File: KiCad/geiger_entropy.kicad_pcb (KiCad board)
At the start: 2 copper layers, 114.5 x 130.5 mm, 34 parts, among them J1 AudioJack2, J2 Jack-DC, J3 ICSP, J4 Conn_01x04_Socket, J5 Conn_01x10_Pin, J6 Conn_01x10_Pin, SW1 RESET, SW2 REV, SW3 FWD, U1 LM393, U2 L7805, U4 ATmega328-P, Y1 16MHz

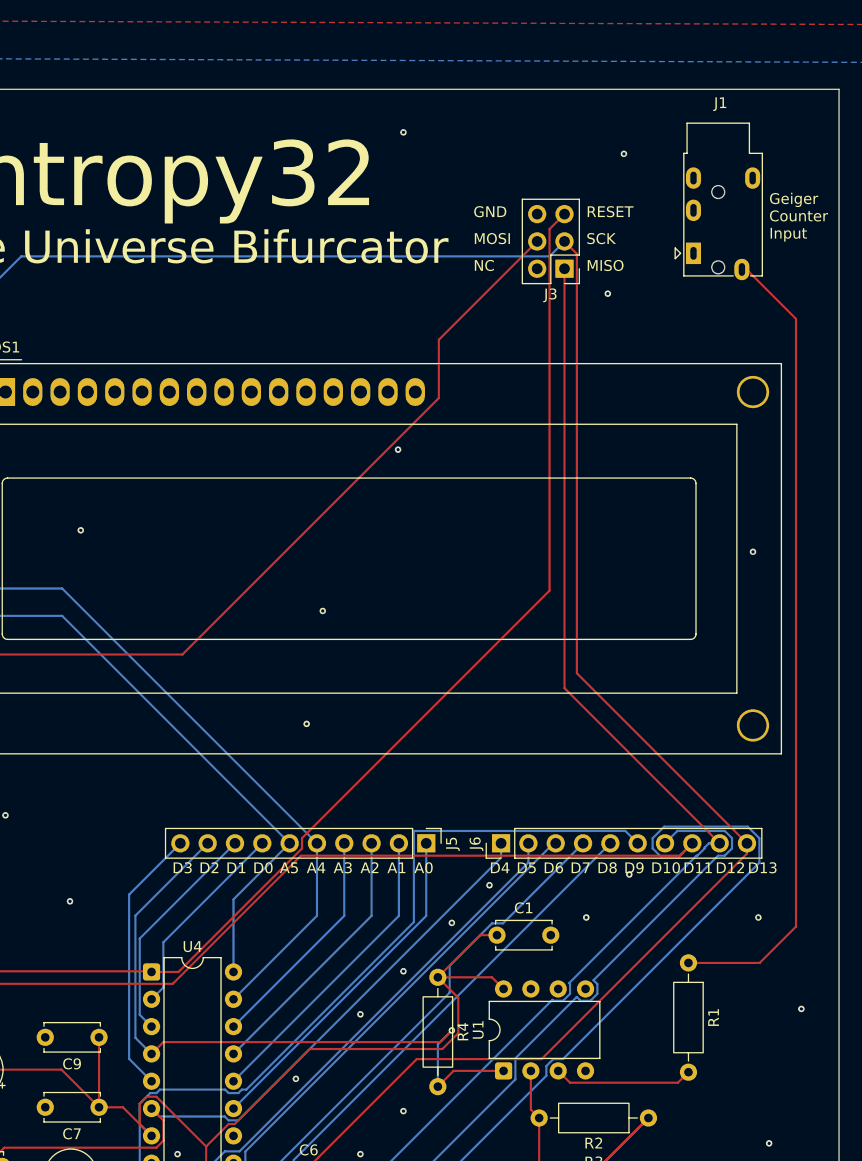
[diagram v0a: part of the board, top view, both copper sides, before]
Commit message: Add BOM and fix signal line debounce issue with a 100pF capacitor - optimise PCB layout
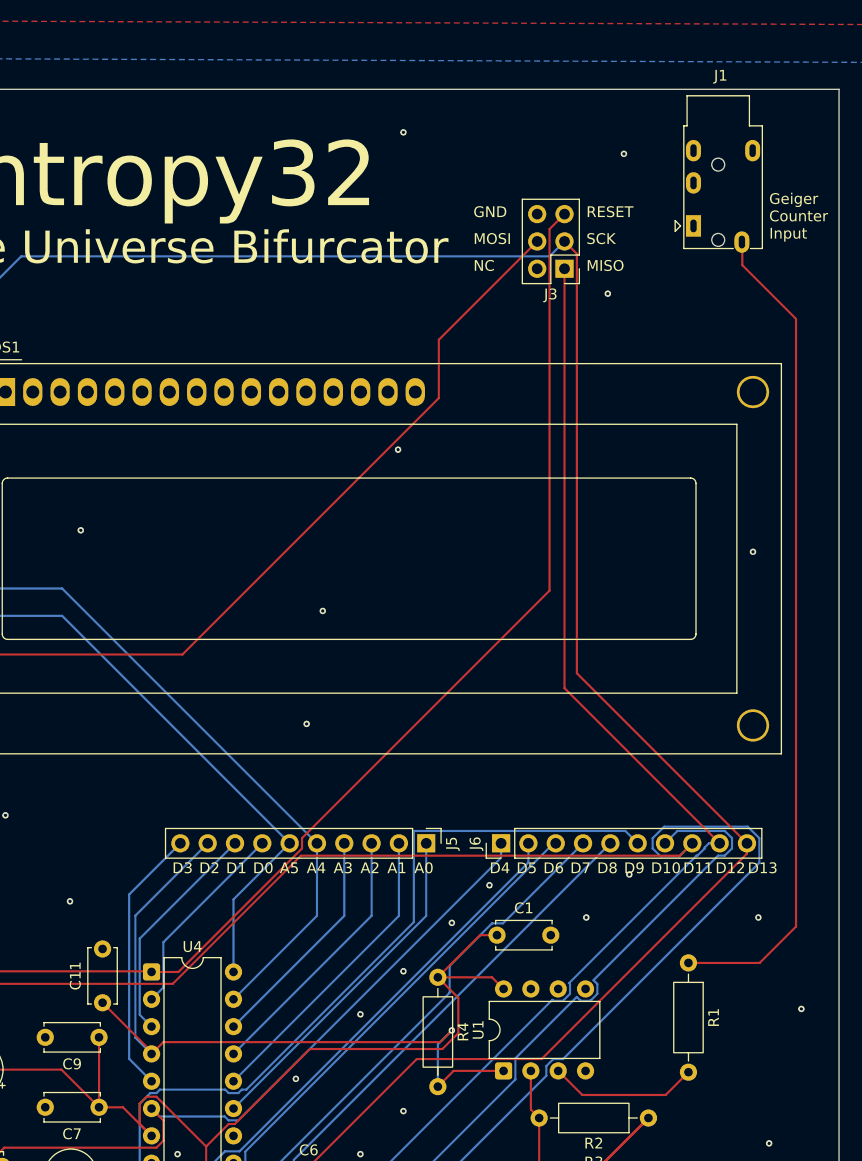
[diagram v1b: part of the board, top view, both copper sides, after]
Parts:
- added C11: 100pF, Capacitor_THT:C_Disc_D5.0mm_W2.5mm_P5.00mm, F.Cu at (79.0, 112.9)
- moved J1 2.55 mm to (134.0, 40.7)
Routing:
- net /D2: track 64.3 -> 70.9 mm
- net Net-(J1-PadS): track 74.8 -> 77.1 mm
- net /Geiger_pulse: track 13.0 -> 13.9 mm
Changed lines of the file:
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@@
 	(footprint "Capacitor_THT:C_Disc_D5.0mm_W2.5mm_P5.00mm"
 		(layer "F.Cu")
+		(at 79.025 112.925 90)
+		(descr "C, Disc series, Radial, pin pitch=5.00mm, diameter*width=5*2.5mm^2, Capacitor, http://cdn-reichelt.de/documents/datenblatt/B300/DS_KERKO_TC.pdf")
+		(tags "C Disc series Radial pin pitch 5.00mm diameter 5mm width 2.5mm Capacitor")
+		(property "Reference" "C11"
+			(at 2.5 -2.5 90)
+			(layer "F.SilkS")
+			(effects
+				(font
+					(size 1 1)
+					(thickness 0.15)
+				)
+			)
+		)
+		(property "Value" "100pF"
+			(at 2.5 2.5 90)
+			(layer "F.Fab")
+			(effects
+				(font
+					(size 1 1)
+					(thickness 0.15)
+				)
+			)
+		)
+		(property "Datasheet" ""
+			(at 0 0 90)
+			(layer "F.Fab")
+			(hide yes)
+			(effects
+				(font
+					(size 1.27 1.27)
+				)
+			)
+		)
+		(property "Description" "Unpolarized capacitor"
+			(at 0 0 90)
+			(layer "F.Fab")
+			(hide yes)
+			(effects
+				(font
+					(size 1.27 1.27)
+				)
+			)
+		)
+		(property "KiLib_Generator" "capacitor/THT/other"
+			(at 0 0 90)
+			(layer "F.SilkS")
+			(hide yes)
+			(effects
+				(font
+					(size 1 1)
+					(thickness 0.15)
+				)
+			)
+		)
+		(property ki_fp_filters "C_*")
+		(sheetname "/")
+		(sheetfile "geiger_entropy.kicad_sch")
+		(units
+			(unit
+				(name "A")
+				(pins "1" "2")
+			)
+		)
+		(attr through_hole)
+		(duplicate_pad_numbers_are_jumpers no)
+		(fp_line
+			(start 5.12 -1.37)
+			(end 5.12 -1.033)
+			(stroke
+				(width 0.12)
+				(type solid)
+			)
+			(layer "F.SilkS")
+		)
+		(fp_line
+			(start -0.12 -1.37)
+			(end 5.12 -1.37)
+			(stroke
+				(width 0.12)
+				(type solid)
+			)
+			(layer "F.SilkS")
+		)
+		(fp_line
+			(start -0.12 -1.033)
+			(end -0.12 -1.37)
+			(stroke
+				(width 0.12)
+				(type solid)
+			)
+			(layer "F.SilkS")
+		)
+		(fp_line
+			(start 5.12 1.033)
+			(end 5.12 1.37)
+			(stroke
+				(width 0.12)
+				(type solid)
+			)
+			(layer "F.SilkS")
+		)
+		(fp_line
+			(start 5.12 1.37)
+			(end -0.12 1.37)
+			(stroke
+				(width 0.12)
+				(type solid)
+			)
+			(layer "F.SilkS")
+		)
+		(fp_line
+			(start -0.12 1.37)
+			(end -0.12 1.033)
+			(stroke
+				(width 0.12)
+				(type solid)
+			)
+			(layer "F.SilkS")
+		)
+		(fp_rect
+			(start -1.05 -1.5)
+			(end 6.05 1.5)
+			(stroke
+				(width 0.05)
+				(type solid)
+			)
+			(fill no)
+			(layer "F.CrtYd")
+		)
+		(fp_rect
+			(start 0 -1.25)
+			(end 5 1.25)
+			(stroke
+				(width 0.1)
+				(type solid)
+			)
+			(fill no)
+			(layer "F.Fab")
+		)
+		(fp_text user "${REFERENCE}"
+			(at 2.5 0 90)
+			(layer "F.Fab")
+			(effects
+				(font
+					(size 1 1)
+					(thickness 0.15)
+				)
+			)
+		)
+		(pad "1" thru_hole circle
+			(at 0 0 90)
+			(size 1.6 1.6)
+			(drill 0.8)
+			(layers "*.Cu" "*.Mask")
+			(remove_unused_layers no)
+			(net "/D2")
+			(pintype "passive")
+		)
+		(pad "2" thru_hole circle
+			(at 5 0 90)
+			(size 1.6 1.6)
+			(drill 0.8)
+			(layers "*.Cu" "*.Mask")
+			(remove_unused_layers no)
+			(net "GND")
+			(pintype "passive")
+		)
+		(embedded_fonts no)
+		(model "${KICAD10_3DMODEL_DIR}/Capacitor_THT.3dshapes/C_Disc_D5.0mm_W2.5mm_P5.00mm.step"
+			(offset
+				(xyz 0 0 0)
+			)
+			(scale
+				(xyz 1 1 1)
+			)
+			(rotate
+				(xyz 0 0 0)
+			)
+		)
+	)
+	(footprint "Capacitor_THT:C_Disc_D5.0mm_W2.5mm_P5.00mm"
+		(layer "F.Cu")
 		(at 69.7 128.1425 180)
 		(descr "C, Disc series, Radial, pin pitch=5.00mm, diameter*width=5*2.5mm^2, Capacitor, http://cdn-reichelt.de/documents/datenblatt/B300/DS_KERKO_TC.pdf")
@@
 	(footprint "Connector_Audio:Jack_3.5mm_PJ320E_Horizontal"
 		(layer "F.Cu")
-		(at 133.9675 43.25)
+		(at 133.9675 40.7)
 		(descr "Headphones with microphone connector, 3.5mm, 4 pins (http://www.qingpu-electronics.com/en/products/WQP-PJ320E-177.html)")
 		(tags "3.5mm jack mic microphone phones headphones 4pins audio plug")
@@
 	)
 	(segment
+		(start 79.025 112.925)
+		(end 83.58 117.48)
+		(width 0.2)
+		(layer "F.Cu")
+		(net "/D2")
+	)
+	(segment
 		(start 111.5 115.5)
 		(end 110.4175 116.5825)
@@
 	)
 	(segment
+		(start 83.58 117.48)
+		(end 83.58 117.6825)
+		(width 0.2)
+		(layer "F.Cu")
+		(net "/D2")
+	)
+	(segment
 		(start 110.4175 116.5825)
 		(end 84.68 116.5825)
@@
 	)
 	(segment
-		(start 138.4675 44.75)
-		(end 138.9075 44.75)
+		(start 143.5 105.8425)
+		(end 140.12 109.2225)
 		(width 0.2)
 		(layer "F.Cu")
@@
 	)
 	(segment
-		(start 133.5 109.2225)
-		(end 140.12 109.2225)
+		(start 138.5 44.3425)
+		(end 143.5 49.3425)
 		(width 0.2)
 		(layer "F.Cu")
@@
 	)
 	(segment
-		(start 143.5 49.3425)
-		(end 143.5 105.8425)
+		(start 140.12 109.2225)
+		(end 133.5 109.2225)
 		(width 0.2)
 		(layer "F.Cu")
@@
 	)
 	(segment
-		(start 138.9075 44.75)
-		(end 143.5 49.3425)
+		(start 138.4675 42.2)
+		(end 138.5 42.2325)
 		(width 0.2)
 		(layer "F.Cu")
@@
 	)
 	(segment
-		(start 140.12 109.2225)
+		(start 138.5 42.2325)
+		(end 138.5 44.3425)
+		(width 0.2)
+		(layer "F.Cu")
+		(net "Net-(J1-PadS)")
+	)
+	(segment
+		(start 143.5 49.3425)
 		(end 143.5 105.8425)
 		(width 0.2)
@@
 	)
 	(segment
-		(start 133.5 119.3825)
-		(end 132.52 120.3625)
+		(start 123.6275 121.5)
+		(end 121.39 119.2625)
 		(width 0.2)
 		(layer "F.Cu")
@@
 	)
 	(segment
-		(start 122.49 120.3625)
-		(end 121.39 119.2625)
+		(start 131.3825 121.5)
+		(end 123.6275 121.5)
 		(width 0.2)
 		(layer "F.Cu")
@@
 	)
 	(segment
-		(start 132.52 120.3625)
-		(end 122.49 120.3625)
+		(start 133.5 119.3825)
+		(end 131.3825 121.5)
 		(width 0.2)
 		(layer "F.Cu")

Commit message: Update PCB
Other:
- board text added: "CAUTION: TRUE RANDOMNESS INSIDE OPERATION MAY CAUSE PARALLEL UNIVERSES"
- board text added: "This device complies with the Heisenberg Uncertainty Principle. Operation is subject to the following: (1) this device may not cause harmful interference with causality, (2) this device must accept any interference received, including unexpected entropy."
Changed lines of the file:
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@@
+		)
+	)
+	(gr_text "This device complies with the Heisenberg Uncertainty Principle. \nOperation is subject to the following: (1) this device may not \ncause harmful interference with causality, (2) this device must \naccept any interference received, including unexpected entropy."
+		(at 66 156.5 0)
+		(layer "F.SilkS")
+		(effects
+			(font
+				(size 1 1)
+				(thickness 0.3)
+				(bold yes)
+			)
+			(justify left bottom)
+		)
+	)
+	(gr_text "CAUTION: TRUE RANDOMNESS INSIDE \nOPERATION MAY CAUSE PARALLEL UNIVERSES"
+		(at 61.5 95.5 0)
+		(layer "F.SilkS")
+		(effects
+			(font
+				(size 1.5 1.5)
+				(thickness 0.3)
+				(bold yes)
+			)
+			(justify left bottom)
 		)
 	)
@@
 	)
 	(via
-		(at 70 95.5)
+		(at 75 87)
 		(size 0.6)
 		(drill 0.3)
@@
 	)
 	(via
-		(at 106.5 61.5)
-		(size 0.6)
-		(drill 0.3)
+		(at 110 65)
+		(size 0.6)
+		(drill 0.3)

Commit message: Update PCB
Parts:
- moved R1 7.58 mm to (140.6, 111.9), turned to -135 degrees
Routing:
- net Net-(J1-PadS): track 77.1 -> 73.0 mm
- net /D2: track 70.9 -> 67.5 mm
- net +5V: track 295.1 -> 297.5 mm

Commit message: Update PCB
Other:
- board text added: "//// 5V LOGIC ////"
- board text added: "//// CAUTION //////////////////// OPERATION MAY CAUSE PARALLEL UNIVERSES"
- board text added: "//// DC //// 9-12V ONLY"
- board text added: "//// WARNING //// GEIGER COUNTER ONLY DO NOT CONNECT AUDIO"
- board text removed: "9-12V DC"
- board text removed: "CAUTION: TRUE RANDOMNESS INSIDE OPERATION MAY CAUSE PARALLEL UNIVERSES"
- board text removed: "Geiger Counter Input"
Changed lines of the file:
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@@
 		(layer "Edge.Cuts")
-	)
-	(gr_text "9-12V \nDC"
-		(at 34 32 0)
-		(layer "F.SilkS")
-		(effects
-			(font
-				(size 1 1)
-				(thickness 0.1)
-			)
-			(justify left bottom)
-		)
 	)
 	(gr_text "D3"
@@
 		)
 	)
-	(gr_text "Geiger \nCounter\nInput"
-		(at 141 42 0)
-		(layer "F.SilkS")
-		(effects
-			(font
-				(size 1 1)
-				(thickness 0.1)
-			)
-			(justify left bottom)
+	(gr_text "This device complies with the Heisenberg Uncertainty Principle. \nOperation is subject to the following: (1) this device may not \ncause harmful interference with causality, (2) this device must \naccept any interference received, including unexpected entropy."
+		(at 66 156.5 0)
+		(layer "F.SilkS")
+		(effects
+			(font
+				(size 1 1)
+				(thickness 0.1)
+				(bold yes)
+			)
+			(justify left bottom)
+		)
+	)
+	(gr_text "//// 5V LOGIC ////"
+		(at 112.5 36 0)
+		(layer "F.SilkS")
+		(effects
+			(font
+				(size 1 1)
+				(thickness 0.1)
+				(bold yes)
+			)
+			(justify left bottom)
+		)
+	)
+	(gr_text "//// DC ////\n9-12V ONLY"
+		(at 36.5 35 90)
+		(layer "F.SilkS")
+		(effects
+			(font
+				(size 1 1)
+				(thickness 0.1)
+			)
+			(justify bottom)
+		)
+	)
+	(gr_text "//// WARNING ////\nGEIGER COUNTER ONLY\nDO NOT CONNECT AUDIO"
+		(at 146 38 90)
+		(layer "F.SilkS")
+		(effects
+			(font
+				(size 1 1)
+				(thickness 0.1)
+			)
+			(justify bottom)
 		)
 	)
@@
 		)
 	)
-	(gr_text "This device complies with the Heisenberg Uncertainty Principle. \nOperation is subject to the following: (1) this device may not \ncause harmful interference with causality, (2) this device must \naccept any interference received, including unexpected entropy."
-		(at 66 156.5 0)
-		(layer "F.SilkS")
-		(effects
-			(font
-				(size 1 1)
-				(thickness 0.3)
-				(bold yes)
-			)
-			(justify left bottom)
-		)
-	)
-	(gr_text "CAUTION: TRUE RANDOMNESS INSIDE \nOPERATION MAY CAUSE PARALLEL UNIVERSES"
+	(gr_text "//// CAUTION ////////////////////\nOPERATION MAY CAUSE PARALLEL UNIVERSES"
 		(at 61.5 95.5 0)
 		(layer "F.SilkS")
 		(effects
 			(font
-				(size 1.5 1.5)
-				(thickness 0.3)
-				(bold yes)
-			)
-			(justify left bottom)
+				(size 1.3 1.3)
+				(thickness 0.1)
+			)
+			(justify left bottom)

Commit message: Update PCB and add hardware license
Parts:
- added REF**: OSHW-Logo_19x20mm_SilkScreen, Symbol:OSHW-Logo_19x20mm_SilkScreen, F.Cu at (47.0, 128.0)
- renumbered C5 to C10, C6 to C2, C7 to C3, C11 to C4, C8 to C5, C9 to C6, C2 to C7, C4 to C8, C3 to C9, J4 to J2, J5 to J3, J6 to J4, J2 to J5, J3 to J6, R2 to R1, R3 to R2, R8 to R3, R1 to R4, R4 to R5, R9 to R6, R6 to R8, R5 to R9, SW2 to SW1, SW3 to SW2, SW1 to SW3, U4 to U2, U2 to U3
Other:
- board text added: "//// CAUTION ////////////////////// OPERATION MAY CREATE PARALLEL UNIVERSES"
- board text removed: "//// CAUTION //////////////////// OPERATION MAY CAUSE PARALLEL UNIVERSES"

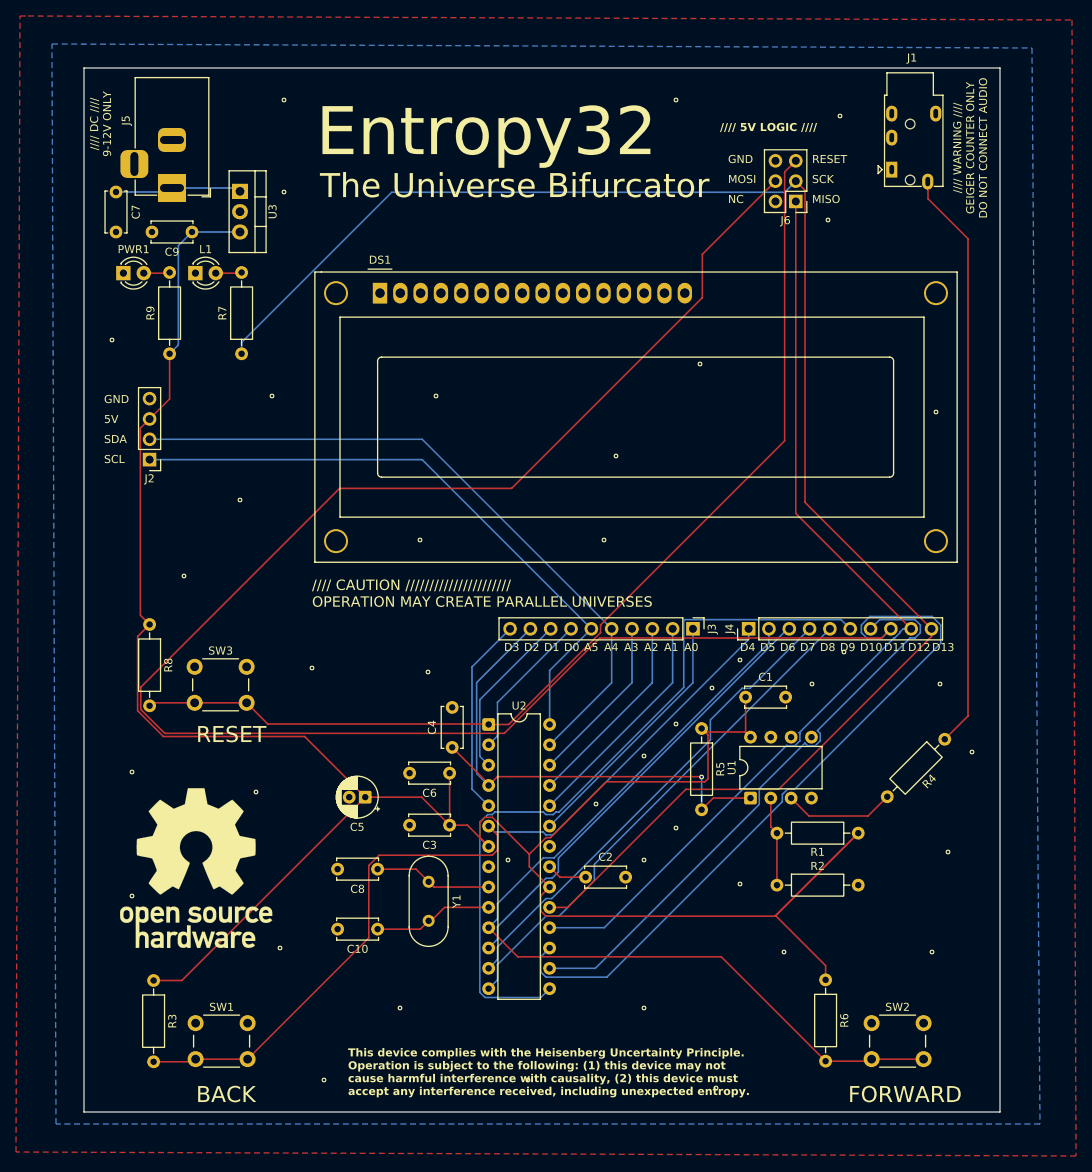
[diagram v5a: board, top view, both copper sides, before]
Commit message: Add wave packet logo and update PCB
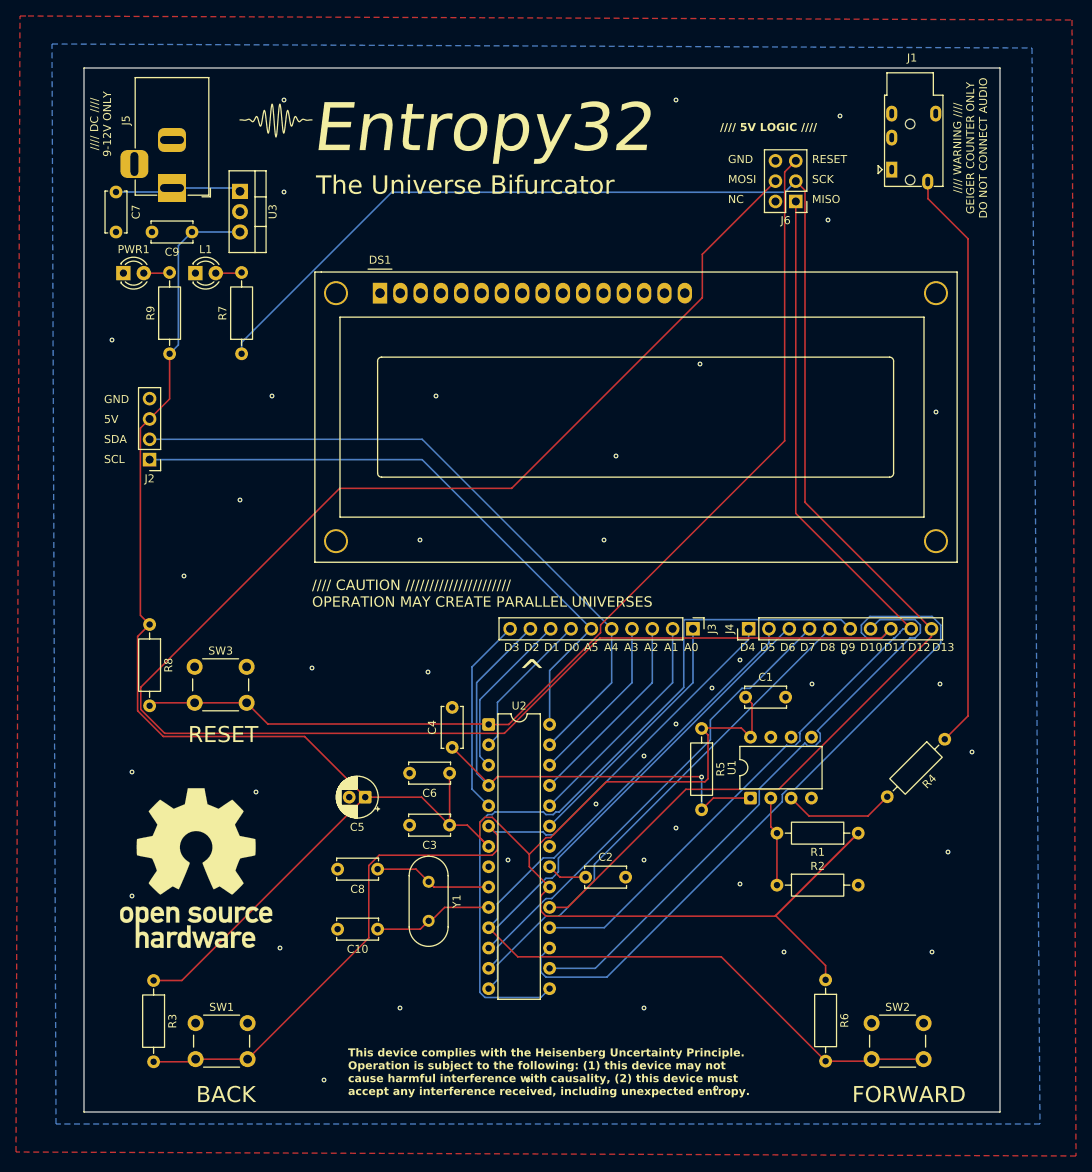
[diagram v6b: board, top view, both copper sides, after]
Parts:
- added ?: LOGO, Entropy32:wave_packet_logo, F.Cu at (57.0, 34.5)
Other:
- board text added: "^"

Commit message: Update PCB and code
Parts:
- moved J2 14.2 mm to (49.0, 88.8)
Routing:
- net +5V: track 297.7 -> 314.0 mm
- net /A4: track 85.3 -> 81.1 mm
- net /D11/MOSI: track 302.0 -> 305.8 mm
- net /A5: track 78.1 -> 74.3 mm
- net /D4: track 107.1 -> 107.9 mm
- net GND: vias 42 -> 59
